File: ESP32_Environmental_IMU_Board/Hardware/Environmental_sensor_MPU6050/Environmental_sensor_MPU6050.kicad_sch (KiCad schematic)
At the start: 0 parts

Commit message: Schematic Completed
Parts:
- added BT1: CH291-1220LF, CH291-1220LF:BAT_CH291-1220LF, symbol CH291-1220LF:CH291-1220LF
- added C1, C2, C8: 10uF, symbol Device:C
- added C10: 10uF, Capacitor_SMD:C_0603_1608Metric, symbol Device:C
- added C11, C12, C13, C14, C16, C4, C5: 0.1uF, Capacitor_SMD:C_0603_1608Metric, symbol Device:C
- added C15: 1uF, symbol Device:C
- added C3, C6, C9: 0.1uF, symbol Device:C
- added C7: 1uF, Capacitor_SMD:C_0603_1608Metric, symbol Device:C
- added D1: MBR0520, Diode_SMD:D_SOD-123, symbol Diode:MBR0520
- added D2, D3, D4, D5: RED_LED, LED_THT:LED_D3.0mm, symbol Device:LED
- added FID1, FID2, FID3: Fiducial, Fiducial:Fiducial_0.75mm_Mask1.5mm, symbol Mechanical:Fiducial
- added J1: USB_C_Receptacle_USB2.0_16P, Connector_USB:USB_C_Receptacle_HCTL_HC-TYPE-C-16P-01A, symbol Connector:USB_C_Receptacle_USB2.0_16P
- added J2, J3: Conn_01x04_Pin, Connector_PinHeader_2.54mm:PinHeader_1x04_P2.54mm_Vertical, symbol Connector:Conn_01x04_Pin
- added J4: Micro_SD_Card, symbol Connector:Micro_SD_Card
- added R1: 0, symbol Device:R
- added R10, R7, R8, R9: 1K, Resistor_SMD:R_0603_1608Metric, symbol Device:R
- added R19, R20, R21, R22: 4.7k, Resistor_SMD:R_0603_1608Metric, symbol Device:R
- added R2: 10k, Resistor_SMD:R_0603_1608Metric, symbol Device:R
- added R23, R24: 0R, Resistor_SMD:R_0603_1608Metric, symbol Device:R
- added R3, R4: 5.1k, Resistor_SMD:R_0603_1608Metric, symbol Device:R
- added R5, R6: 22, Resistor_SMD:R_0603_1608Metric, symbol Device:R
- added SW1: SW_Push, Button_Switch_THT:SW_PUSH_6mm, symbol Switch:SW_Push
- added SW2: SW_Push, Button_Switch_SMD:SW_Push_SPST_NO_Alps_SKRK, symbol Switch:SW_Push
- added TP1: TP_EN, Test Point:TestPoint_Pad_D2.5mm, symbol Connector:TestPoint
- added TP2: TP_BOOT, Test Point:TestPoint_Pad_D2.5mm, symbol Connector:TestPoint
- added TP3: TP_TX, Test Point:TestPoint_Pad_D2.5mm, symbol Connector:TestPoint
- added TP4: TP_RX, Test Point:TestPoint_Pad_D2.5mm, symbol Connector:TestPoint
- added TP5: TP_SDA, symbol Connector:TestPoint
- added TP6: TP_SCL, symbol Connector:TestPoint
- added TP7: TP_3V3, symbol Connector:TestPoint
- added TP8: TP_GND, symbol Connector:TestPoint
- added U1: AP2112K-3.3, Package_TO_SOT_SMD:SOT-23-5, symbol Regulator_Linear:AP2112K-3.3
- added U2: ESP32-S3-WROOM-1, RF_Module:ESP32-S3-WROOM-1, symbol RF_Module:ESP32-S3-WROOM-1
- added U3: USBLC6-2P6, Package_TO_SOT_SMD:SOT-666, symbol Power_Protection:USBLC6-2P6
- added U4: MPU-6050, Sensor_Motion:InvenSense_QFN-24_4x4mm_P0.5mm, symbol Sensor_Motion:MPU-6050
- added U5: BME280, Package_LGA:Bosch_LGA-8_2.5x2.5mm_P0.65mm_ClockwisePinNumbering, symbol Sensor:BME280
- added U6: DS3231M, Package_SO:SOIC-16W_7.5x10.3mm_P1.27mm, symbol Timer_RTC:DS3231M
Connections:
- new net: D5.2 (A), R10.1
- new net: D2.2 (A), R7.1
- new net: BT1.P, U6.14 (VBAT)
- new net: J3.3 (Pin_3), R19.1, R21.2, R23.1, TP6.1
- new net: J3.4 (Pin_4), R20.1, R22.2, R24.1, TP5.1
- new net: TP4.1, U2.36 (RXD0)
- new net: TP3.1, U2.37 (TXD0)
- new net: C13.1, U4.10 (REGOUT)
- new net: D4.2 (A), R9.1
- new net: J1.B5 (CC2), R4.1
- new net: J1.A5 (CC1), R3.1
- new net: D3.2 (A), R8.1
- new net +3.3V: C12.1, C14.1, C15.1, C16.1, C2.1, C6.1, C8.1, C9.1, J2.2 (Pin_2), J3.2 (Pin_2), J4.4 (VDD), R1.1, R1.2, R2.1, R21.1, R22.1, R7.2, TP7.1, U1.5 (VOUT), U2.2 (3V3), U4.13 (VDD), U4.8 (VLOGIC), U4.9 (AD0), U5.2 (CSB), U5.8 (VDD), U6.2 (VCC)
- new net +5V: C1.1, C3.1, D1.1 (K), U1.1 (VIN)
- new net 5V: D1.2 (A), U1.3 (EN)
- new net ACT_LED: R9.2, U2.5 (IO5)
- new net BOOT: C5.2, SW2.2, TP2.1, U2.27 (IO0)
- new net CHIP-PU/RST/EN: C4.2, C7.1, R2.2, SW1.2, TP1.1, U2.3 (EN)
- new net CS: J4.2 (DAT3/CD), U2.18 (IO10)
- new net D+: J1.A6 (D+), J1.B6 (D+), U3.3 (I/O2)
- new net D-: J1.A7 (D-), J1.B7 (D-), U3.1 (I/O1)
- new net ERR_LED: R10.2, U2.6 (IO6)
- new net GND: BT1.N, C1.2, C10.2, C11.2, C12.2, C13.2, C14.2, C15.2, C16.2, C2.2, C3.2, C4.1, C5.1, C6.2, C7.2, C8.2, C9.2, D2.1 (K), D3.1 (K), D4.1 (K), D5.1 (K), J1.A1 (GND), J1.A12 (GND), J1.B1 (GND), J1.B12 (GND), J1.S1 (SHIELD), J2.1 (Pin_1), J3.1 (Pin_1), J4.6 (VSS), R3.2, R4.2, SW1.1, SW2.1, TP8.1, U1.2 (GND), U2.1 (GND), U2.40 (GND), U2.41 (GND), U3.2 (GND), U4.18 (GND), U5.1 (GND), U5.5 (SDO), U5.7 (GND), U6.10 (GND), U6.11 (GND), U6.12 (GND), U6.13 (GND), U6.5 (GND), U6.6 (GND), U6.7 (GND), U6.8 (GND), U6.9 (GND)
- new net MISO: J4.7 (DAT0), U2.21 (IO13)
- new net MOSI: J4.3 (CMD), U2.19 (IO11)
- new net N: R5.1, U3.6 (I/O1)
- new net P: R6.1, U3.4 (I/O2)
- new net SCK: J4.5 (CLK), U2.20 (IO12)
- new net SCL2/IO18: R23.2, U2.11 (IO18)
- new net SCL/IO9: J2.3 (Pin_3), R19.2, U2.17 (IO9), U4.23 (SCL), U5.4 (SCK), U6.16 (SCL)
- new net SDA2/IO17: R24.2, U2.10 (IO17)
- new net SDA/IO8: J2.4 (Pin_4), R20.2, U2.12 (IO8), U4.24 (SDA), U5.3 (SDI), U6.15 (SDA)
- new net STATUS_LED: R8.2, U2.4 (IO4)
- new net USB_D+: R6.2, U2.14 (USB_D+)
- new net USB_D-: R5.2, U2.13 (USB_D-)
- new net VBUS: C10.1, C11.1, J1.A4 (VBUS), J1.A9 (VBUS), J1.B4 (VBUS), J1.B9 (VBUS), U3.5 (VBUS)
- no-connect marks 0 -> 31
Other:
- note added: "BME280 SENSOR"
- note added: "FIDUCIAL"
- note added: "I2C CONNECTOR"
- note added: "INDICATION LEDS"
- note added: "LDO"
- note added: "MICROCONTROLLER"
- note added: "MICROSSD"
- note added: "MPU6050 SENSOR"
- note added: "OLED"
- note added: "RTC"
- note added: "USB CONTROLLER"
- title: (none) -> ESP32_Custom_Sensor_Board

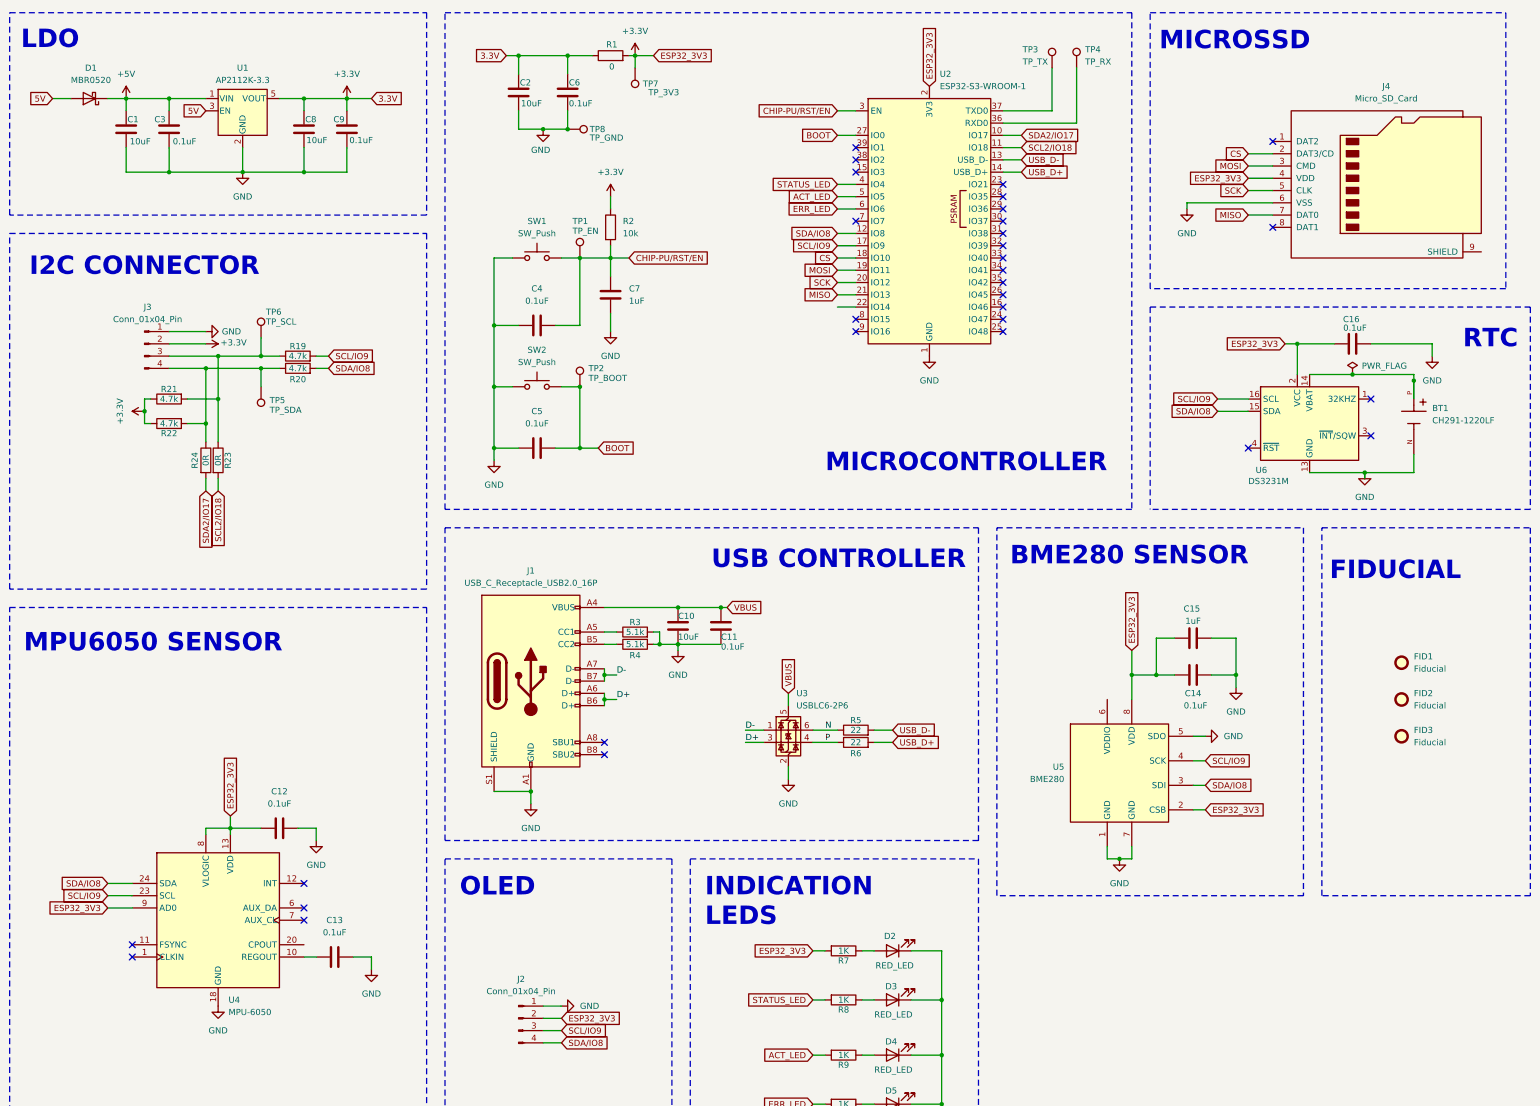
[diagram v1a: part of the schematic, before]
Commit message: Footprints assigned
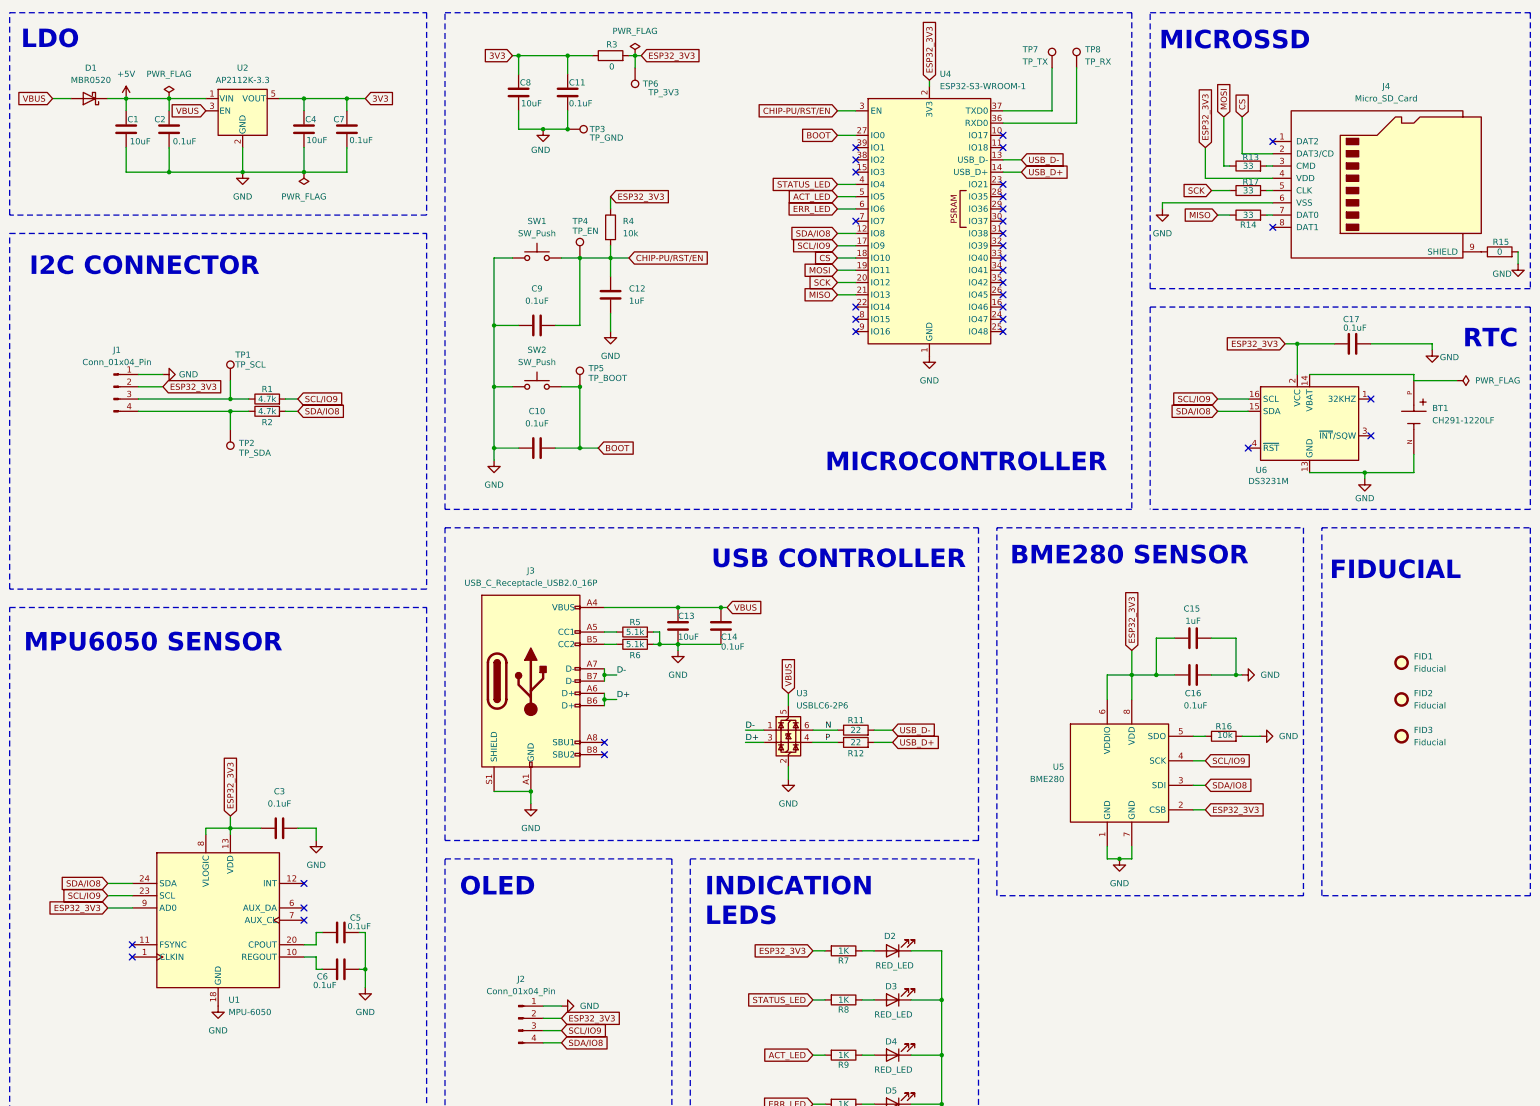
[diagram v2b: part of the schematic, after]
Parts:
- removed R21, R22: 4.7k, Resistor_SMD:R_0603_1608Metric, symbol Device:R
- removed R23, R24: 0R, Resistor_SMD:R_0603_1608Metric, symbol Device:R
- added C5: 0.1uF, Capacitor_SMD:C_0603_1608Metric, symbol Device:C
- added R13, R14, R17: 33, Resistor_SMD:R_0603_1608Metric, symbol Device:R
- added R15: 0, Resistor_SMD:R_0603_1608Metric, symbol Device:R
- added R16: 10k, Resistor_SMD:R_0603_1608Metric, symbol Device:R
- C1: footprint (none) -> Capacitor_SMD:C_0805_2012Metric
- C11: renamed from C6; footprint (none) -> Capacitor_SMD:C_0603_1608Metric
- C13: renamed from C10; footprint Capacitor_SMD:C_0603_1608Metric -> Capacitor_SMD:C_0805_2012Metric
- C15: footprint (none) -> Capacitor_SMD:C_0603_1608Metric
- C2: renamed from C3; footprint (none) -> Capacitor_SMD:C_0603_1608Metric
- C4: renamed from C8; footprint (none) -> Capacitor_SMD:C_0805_2012Metric
- C7: renamed from C9; footprint (none) -> Capacitor_SMD:C_0603_1608Metric
- C8: renamed from C2; footprint (none) -> Capacitor_SMD:C_0805_2012Metric
- D2, D3, D4, D5: footprint LED_THT:LED_D3.0mm -> LED_SMD:LED_0201_0603Metric
- J4: footprint (none) -> Connector_Card:microSD_HC_Hirose_DM3AT-SF-PEJM5
- R3: renamed from R1; footprint (none) -> Resistor_SMD:R_0603_1608Metric
- SW1: footprint Button_Switch_THT:SW_PUSH_6mm -> Button_Switch_SMD:SW_Push_SPST_NO_Alps_SKRK
- TP1: renamed from TP6; footprint (none) -> Test Point:TestPoint_Pad_D2.5mm
- TP2: renamed from TP5; footprint (none) -> Test Point:TestPoint_Pad_D2.5mm
- TP3: renamed from TP8; footprint (none) -> Test Point:TestPoint_Pad_D2.5mm
- TP6: renamed from TP7; footprint (none) -> Test Point:TestPoint_Pad_D2.5mm
- renumbered C5 to C10, C7 to C12, C11 to C14, C14 to C16, C16 to C17, C12 to C3, C13 to C6, C4 to C9, J3 to J1, J1 to J3, R19 to R1, R5 to R11, R6 to R12, R20 to R2, R2 to R4, R3 to R5, R4 to R6, TP1 to TP4, TP2 to TP5, TP3 to TP7, TP4 to TP8, U4 to U1, U1 to U2, U2 to U4
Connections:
- net 5V is gone; now on net VBUS: D1.2 (A), U2.3 (EN)
- net GND: now also C5.2, R15.2, R16.2; no longer U5.5 (SDO)
- net MISO: now also R14.1; no longer J4.7 (DAT0)
- net MOSI: now also R13.1; no longer J4.3 (CMD)
- net SCK: now also R17.1; no longer J4.5 (CLK)
- net at J4.9 (SHIELD): now also R15.1
- net ESP32_3V3: now reaches U5.6 (VDDIO)
- net ESP32_3V3: now also C15.1, C16.1, C17.1, C3.1, J1.2 (Pin_2), J2.2 (Pin_2), J4.4 (VDD), R3.2, R4.1, R7.2, TP6.1, U1.13 (VDD), U1.8 (VLOGIC), U1.9 (AD0), U4.2 (3V3), U5.2 (CSB), U5.8 (VDD), U6.2 (VCC)
- net at U1.20 (CPOUT): now also C5.1
- removed net +3.3V: C11.1, C15.1, C16.1, C17.1, C3.1, C4.1, C7.1, C8.1, J1.2 (Pin_2), J2.2 (Pin_2), J4.4 (VDD), R3.1, R3.2, R4.1, R7.2, TP6.1, U1.13 (VDD), U1.8 (VLOGIC), U1.9 (AD0), U2.5 (VOUT), U4.2 (3V3), U5.2 (CSB), U5.8 (VDD), U6.2 (VCC)
- net SCL2/IO18: no longer names the net of U4.11 (IO18)
- net SDA2/IO17: no longer names the net of U4.10 (IO17)
- new net: R16.1, U5.5 (SDO)
- new net: J4.3 (CMD), R13.2
- new net: J4.5 (CLK), R17.2
- new net: J4.7 (DAT0), R14.2
- new net 3V3: C11.1, C4.1, C7.1, C8.1, R3.1, U2.5 (VOUT)
- no-connect marks 31 -> 34
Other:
- moved on the sheet: C6, J1, R1, R2, TP1, TP2

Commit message: Schematic reaaranged, Board setup loaded
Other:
- moved on the sheet: C13, C14, C3, C5, C6, J1, J3, R1, R11, R12, R2, R5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

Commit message: PCB layout started
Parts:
- removed C3, C5, C6: 0.1uF, Capacitor_SMD:C_0603_1608Metric, symbol Device:C
- removed TP1: TP_SCL, Test Point:TestPoint_Pad_D2.5mm, symbol Connector:TestPoint
- removed TP2: TP_SDA, Test Point:TestPoint_Pad_D2.5mm, symbol Connector:TestPoint
- removed TP4: TP_EN, Test Point:TestPoint_Pad_D2.5mm, symbol Connector:TestPoint
- removed TP5: TP_BOOT, Test Point:TestPoint_Pad_D2.5mm, symbol Connector:TestPoint
- removed U1: MPU-6050, Sensor_Motion:InvenSense_QFN-24_4x4mm_P0.5mm, symbol Sensor_Motion:MPU-6050
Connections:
- no-connect marks 34 -> 29
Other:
- note removed: "MPU6050 SENSOR"
- moved on the sheet: BT1, C1, C10, C11, C12, C13, C14, C15, C16, C17, C2, C4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
